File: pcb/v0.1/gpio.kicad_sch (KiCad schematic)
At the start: 36 parts, among them J7 ComputeModule5-CM5_connector, J8 Micro_SD_molex, J9 AudioJack3, SW1 SW_Push_45deg, U4 PCM5102A, U5 RT9742GGJ5, U6 RT9742GGJ5

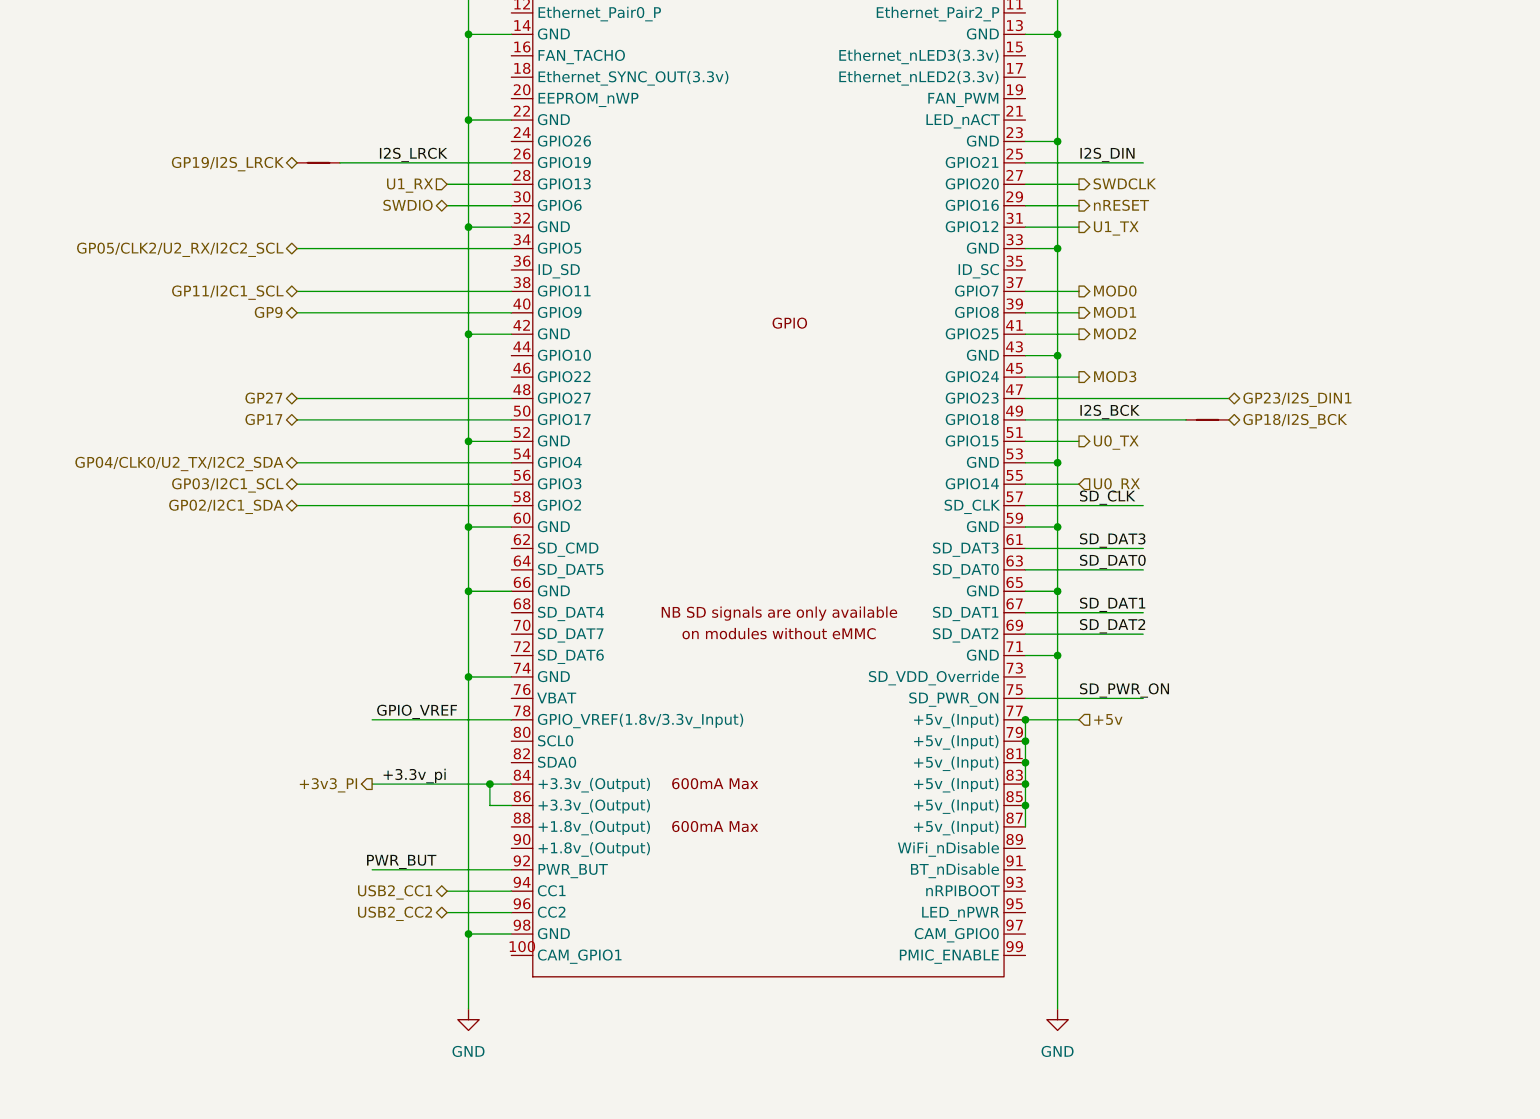
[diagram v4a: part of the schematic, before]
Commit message: Fix display connector wiring
Was not linked up with the i2c and CAM_GPIO pins from the gpio page.
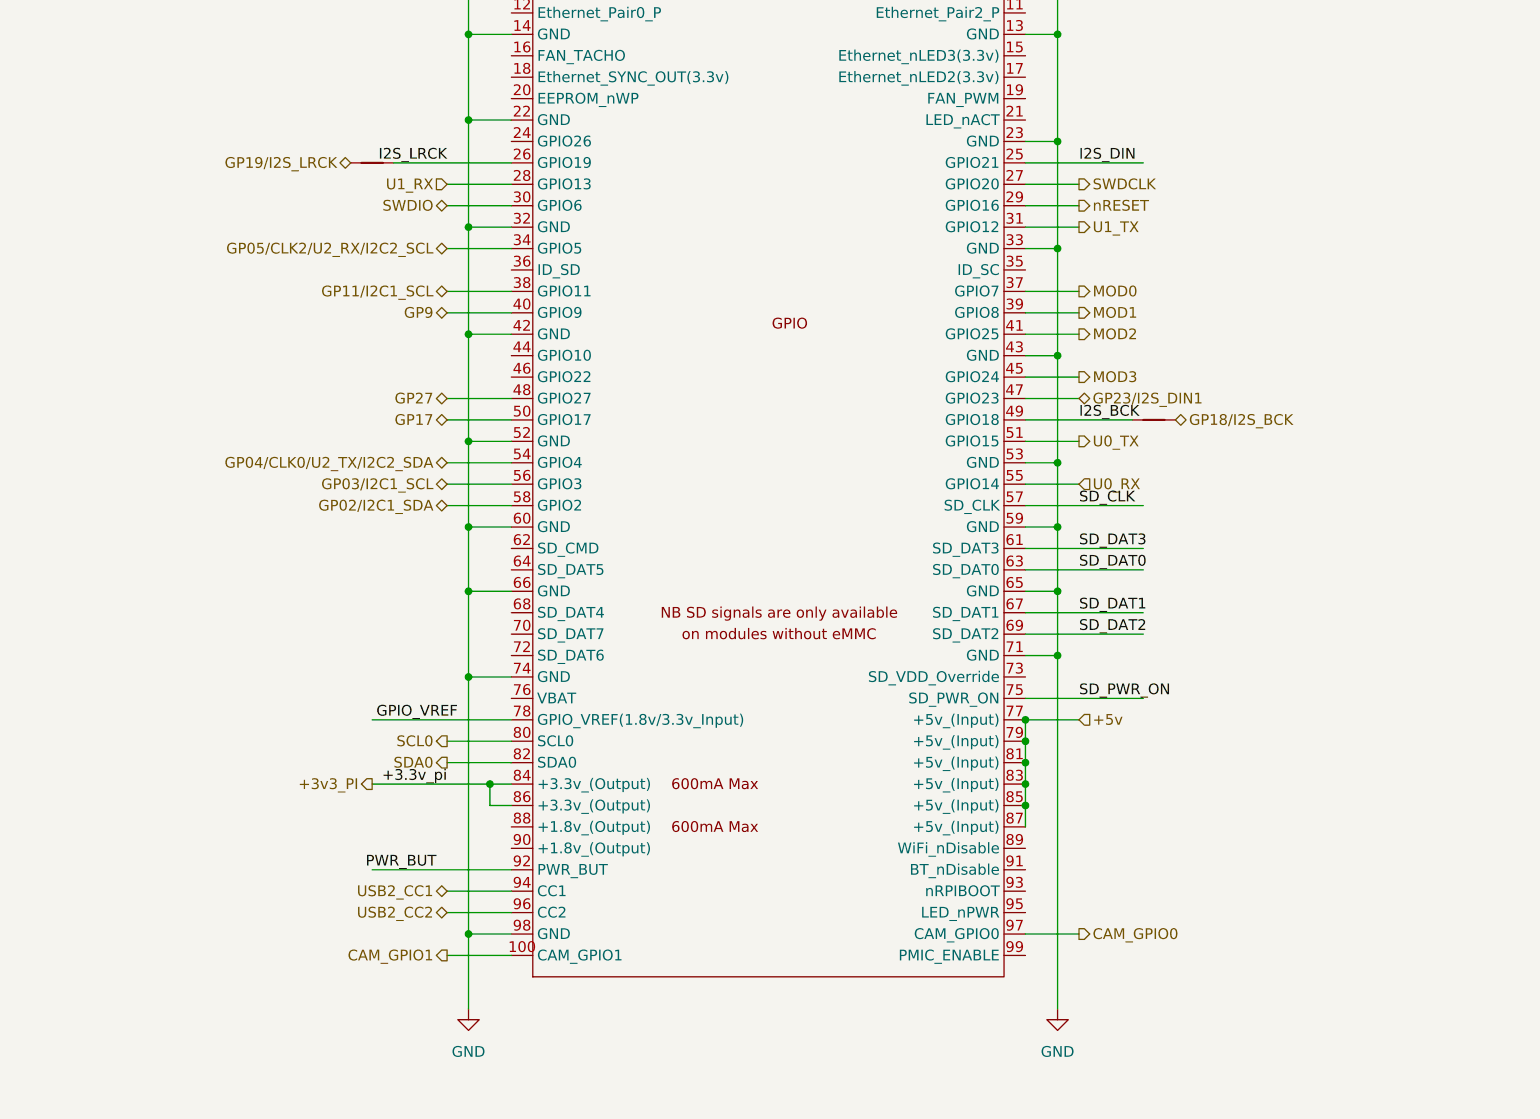
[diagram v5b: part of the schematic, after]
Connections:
- net CAM_GPIO1: now reaches J7.100 (CAM_GPIO1)
- net SCL0: now reaches J7.80 (SCL0)
- net SDA0: now reaches J7.82 (SDA0)
- net CAM_GPIO0: now reaches J7.97 (CAM_GPIO0)
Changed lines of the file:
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@@
 	(wire
 		(pts
-			(xy 69.85 124.46) (xy 95.25 124.46)
+			(xy 87.63 124.46) (xy 95.25 124.46)
 		)
 		(stroke
@@
 	(wire
 		(pts
-			(xy 74.93 93.98) (xy 95.25 93.98)
+			(xy 81.28 93.98) (xy 95.25 93.98)
 		)
 		(stroke
@@
 	(wire
 		(pts
+			(xy 87.63 187.96) (xy 95.25 187.96)
+		)
+		(stroke
+			(width 0)
+			(type default)
+		)
+	)
+	(wire
+		(pts
 			(xy 293.37 220.98) (xy 293.37 222.25)
 		)
@@
 	(wire
 		(pts
-			(xy 69.85 109.22) (xy 95.25 109.22)
+			(xy 87.63 109.22) (xy 95.25 109.22)
 		)
 		(stroke
@@
 	(wire
 		(pts
-			(xy 156.21 124.46) (xy 175.26 124.46)
+			(xy 156.21 124.46) (xy 168.91 124.46)
 		)
 		(stroke
@@
 	(wire
 		(pts
-			(xy 69.85 134.62) (xy 95.25 134.62)
+			(xy 87.63 134.62) (xy 95.25 134.62)
 		)
 		(stroke
@@
 	(wire
 		(pts
+			(xy 87.63 162.56) (xy 95.25 162.56)
+		)
+		(stroke
+			(width 0)
+			(type default)
+		)
+	)
+	(wire
+		(pts
 			(xy 300.99 203.2) (xy 309.88 203.2)
 		)
@@
 	(wire
 		(pts
+			(xy 156.21 185.42) (xy 162.56 185.42)
+		)
+		(stroke
+			(width 0)
+			(type default)
+		)
+	)
+	(wire
+		(pts
 			(xy 346.71 152.4) (xy 346.71 162.56)
 		)
@@
 	(wire
 		(pts
-			(xy 69.85 129.54) (xy 95.25 129.54)
+			(xy 87.63 129.54) (xy 95.25 129.54)
 		)
 		(stroke
@@
 	(wire
 		(pts
-			(xy 69.85 111.76) (xy 95.25 111.76)
+			(xy 87.63 111.76) (xy 95.25 111.76)
 		)
 		(stroke
@@
 	(wire
 		(pts
-			(xy 69.85 104.14) (xy 95.25 104.14)
+			(xy 87.63 104.14) (xy 95.25 104.14)
 		)
 		(stroke
@@
 	(wire
 		(pts
-			(xy 69.85 132.08) (xy 95.25 132.08)
+			(xy 87.63 132.08) (xy 95.25 132.08)
 		)
 		(stroke
@@
 	(wire
 		(pts
-			(xy 69.85 121.92) (xy 95.25 121.92)
+			(xy 87.63 121.92) (xy 95.25 121.92)
 		)
 		(stroke
@@
 	(wire
 		(pts
-			(xy 156.21 121.92) (xy 180.34 121.92)
+			(xy 156.21 121.92) (xy 162.56 121.92)
 		)
 		(stroke
@@
 	(wire
 		(pts
+			(xy 87.63 165.1) (xy 95.25 165.1)
+		)
+		(stroke
+			(width 0)
+			(type default)
+		)
+	)
+	(wire
+		(pts
 			(xy 369.57 104.14) (xy 369.57 106.68)
 		)
@@
 		)
 	)
+	(hierarchical_label "SDA0"
+		(shape output)
+		(at 87.63 165.1 180)
+		(effects
+			(font
+				(size 1.27 1.27)
+			)
+			(justify right)
+		)
+	)
 	(hierarchical_label "U1_TX"
 		(shape output)
@@
 		)
 	)
+	(hierarchical_label "CAM_GPIO1"
+		(shape output)
+		(at 87.63 187.96 180)
+		(effects
+			(font
+				(size 1.27 1.27)
+			)
+			(justify right)
+		)
+	)
 	(hierarchical_label "GP27"
 		(shape bidirectional)
-		(at 69.85 121.92 180)
+		(at 87.63 121.92 180)
 		(effects
 			(font
@@
 	(hierarchical_label "GP05{slash}CLK2{slash}U2_RX{slash}I2C2_SCL"
 		(shape bidirectional)
-		(at 69.85 104.14 180)
+		(at 87.63 104.14 180)
 		(effects
 			(font
@@
 	(hierarchical_label "GP9"
 		(shape bidirectional)
-		(at 69.85 111.76 180)
+		(at 87.63 111.76 180)
 		(effects
 			(font
@@
 	(hierarchical_label "GP11{slash}I2C1_SCL"
 		(shape bidirectional)
-		(at 69.85 109.22 180)
+		(at 87.63 109.22 180)
 		(effects
 			(font
@@
 	(hierarchical_label "GP02{slash}I2C1_SDA"
 		(shape bidirectional)
-		(at 69.85 134.62 180)
+		(at 87.63 134.62 180)
 		(effects
 			(font
@@
 	(hierarchical_label "GP18{slash}I2S_BCK"
 		(shape bidirectional)
-		(at 180.34 124.46 0)
+		(at 173.99 124.46 0)
 		(effects
 			(font
@@
 	(hierarchical_label "GP04{slash}CLK0{slash}U2_TX{slash}I2C2_SDA"
 		(shape bidirectional)
-		(at 69.85 129.54 180)
+		(at 87.63 129.54 180)
 		(effects
 			(font
@@
 	(hierarchical_label "GP17"
 		(shape bidirectional)
-		(at 69.85 124.46 180)
+		(at 87.63 124.46 180)
 		(effects
 			(font
@@
 		)
 	)
+	(hierarchical_label "SCL0"
+		(shape output)
+		(at 87.63 162.56 180)
+		(effects
+			(font
+				(size 1.27 1.27)
+			)
+			(justify right)
+		)
+	)
+	(hierarchical_label "CAM_GPIO0"
+		(shape output)
+		(at 162.56 185.42 0)
+		(effects
+			(font
+				(size 1.27 1.27)
+			)
+			(justify left)
+		)
+	)
 	(hierarchical_label "GP23{slash}I2S_DIN1"
 		(shape bidirectional)
-		(at 180.34 121.92 0)
+		(at 162.56 121.92 0)
 		(effects
 			(font
@@
 	(hierarchical_label "GP03{slash}I2C1_SCL"
 		(shape bidirectional)
-		(at 69.85 132.08 180)
+		(at 87.63 132.08 180)
 		(effects
 			(font
@@
 	(hierarchical_label "GP19{slash}I2S_LRCK"
 		(shape bidirectional)
-		(at 69.85 93.98 180)
+		(at 76.2 93.98 180)
 		(effects
 			(font
@@
 	(symbol
 		(lib_id "Device:NetTie_2")
-		(at 177.8 124.46 0)
+		(at 171.45 124.46 0)
 		(unit 1)
 		(body_style 1)
@@
 		(fields_autoplaced yes)
 		(property "Reference" "NT1"
-			(at 177.8 119.38 0)
+			(at 171.45 119.38 0)
 			(hide yes)
 			(show_name no)
@@
 		)
 		(property "Value" "NetTie_2"
-			(at 177.8 121.92 0)
+			(at 171.45 121.92 0)
 			(hide yes)
 			(show_name no)
@@
 		)
 		(property "Footprint" ""
-			(at 177.8 124.46 0)
+			(at 171.45 124.46 0)
 			(hide yes)
 			(show_name no)
@@
 		)
 		(property "Datasheet" ""
-			(at 177.8 124.46 0)
+			(at 171.45 124.46 0)
 			(hide yes)
 			(show_name no)
@@
 		)
 		(property "Description" "Net tie, 2 pins"
-			(at 177.8 124.46 0)
+			(at 171.45 124.46 0)
 			(hide yes)
 			(show_name no)
@@
 	(symbol
 		(lib_id "Device:NetTie_2")
-		(at 72.39 93.98 0)
+		(at 78.74 93.98 0)
 		(mirror y)
 		(unit 1)
@@
 		(fields_autoplaced yes)
 		(property "Reference" "NT2"
-			(at 72.39 88.9 0)
+			(at 78.74 88.9 0)
 			(hide yes)
 			(show_name no)
@@
 		)
 		(property "Value" "NetTie_2"
-			(at 72.39 91.44 0)
+			(at 78.74 91.44 0)
 			(hide yes)
 			(show_name no)
@@
 		)
 		(property "Footprint" ""
-			(at 72.39 93.98 0)
+			(at 78.74 93.98 0)
 			(hide yes)
 			(show_name no)
@@
 		)
 		(property "Datasheet" ""
-			(at 72.39 93.98 0)
+			(at 78.74 93.98 0)
 			(hide yes)
 			(show_name no)
@@
 		)
 		(property "Description" "Net tie, 2 pins"
-			(at 72.39 93.98 0)
+			(at 78.74 93.98 0)
 			(hide yes)
 			(show_name no)

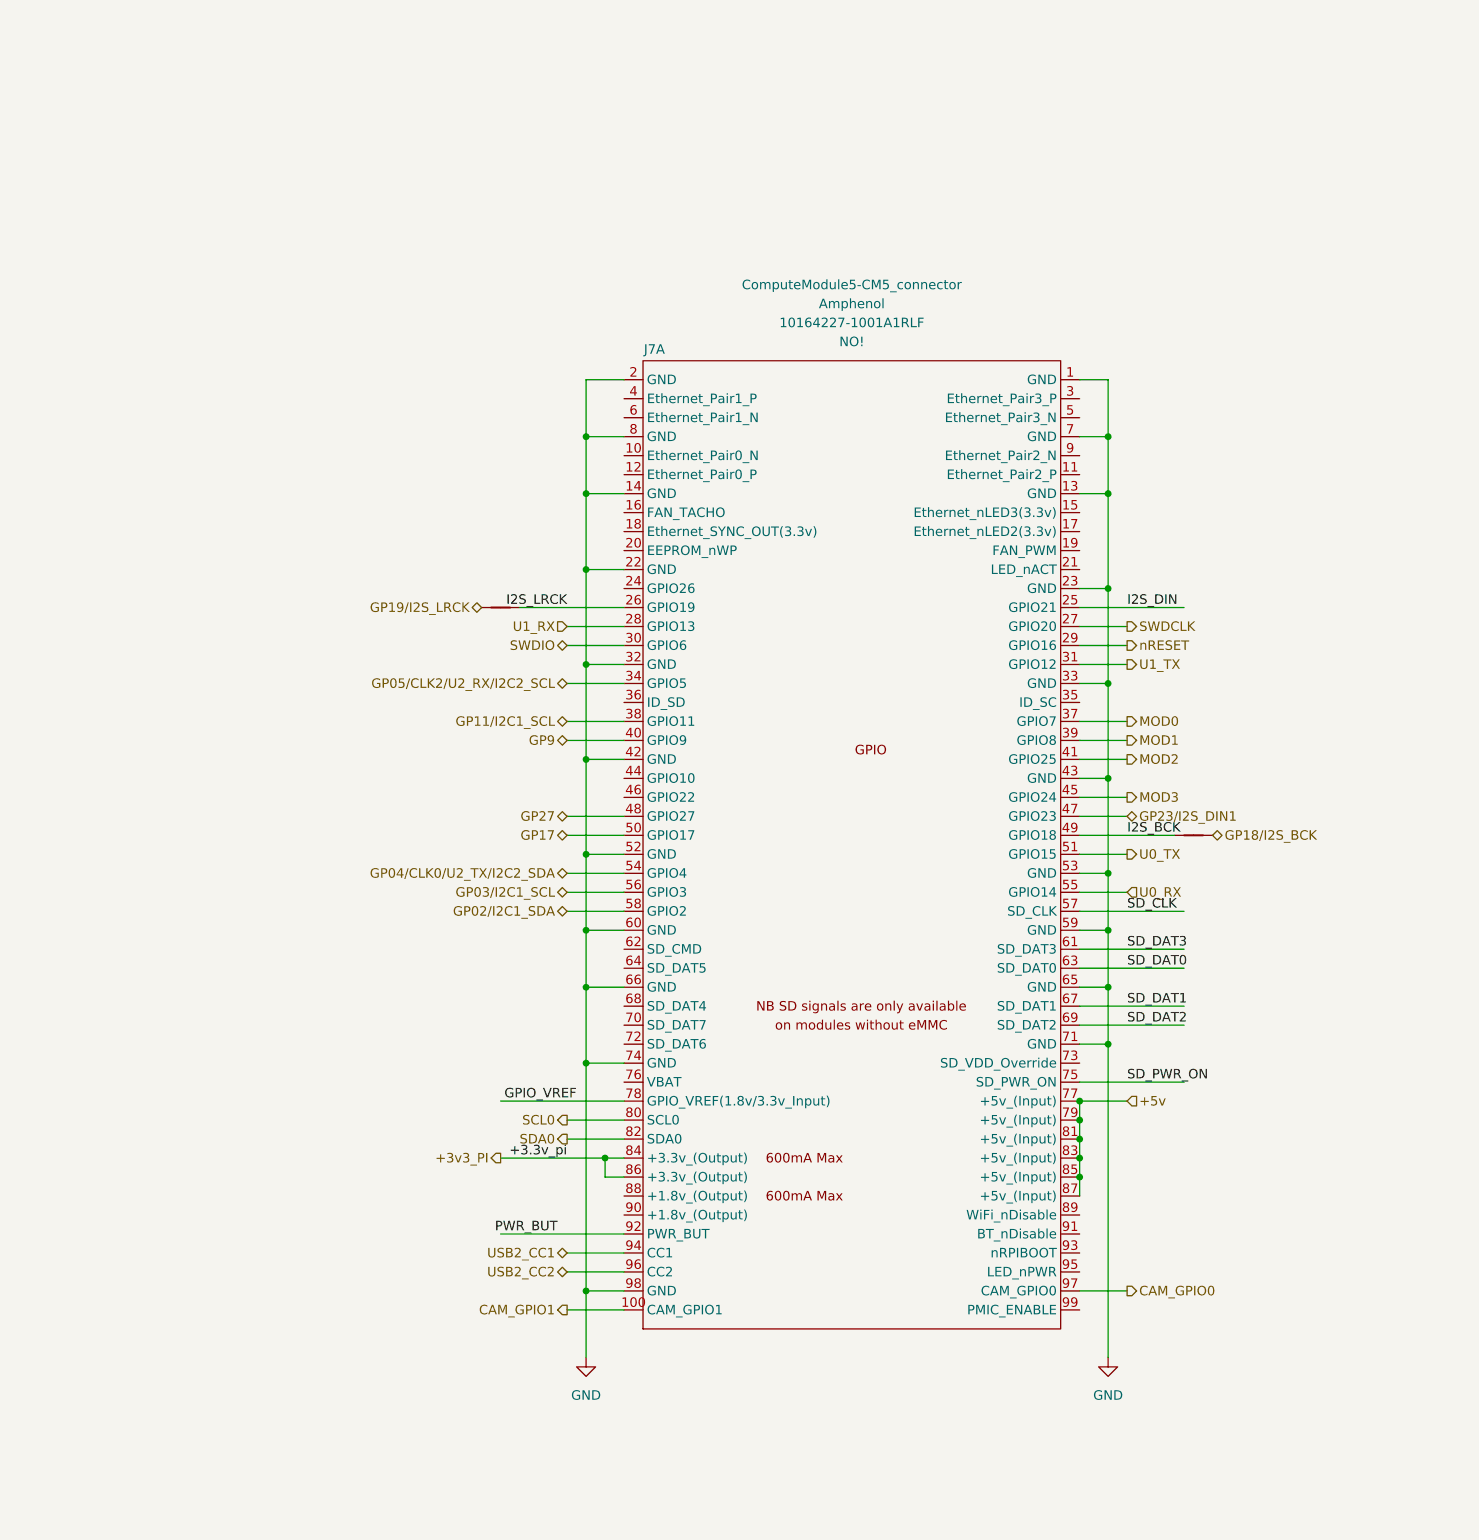
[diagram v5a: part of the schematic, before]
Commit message: High speed and Super speed ESD arrays
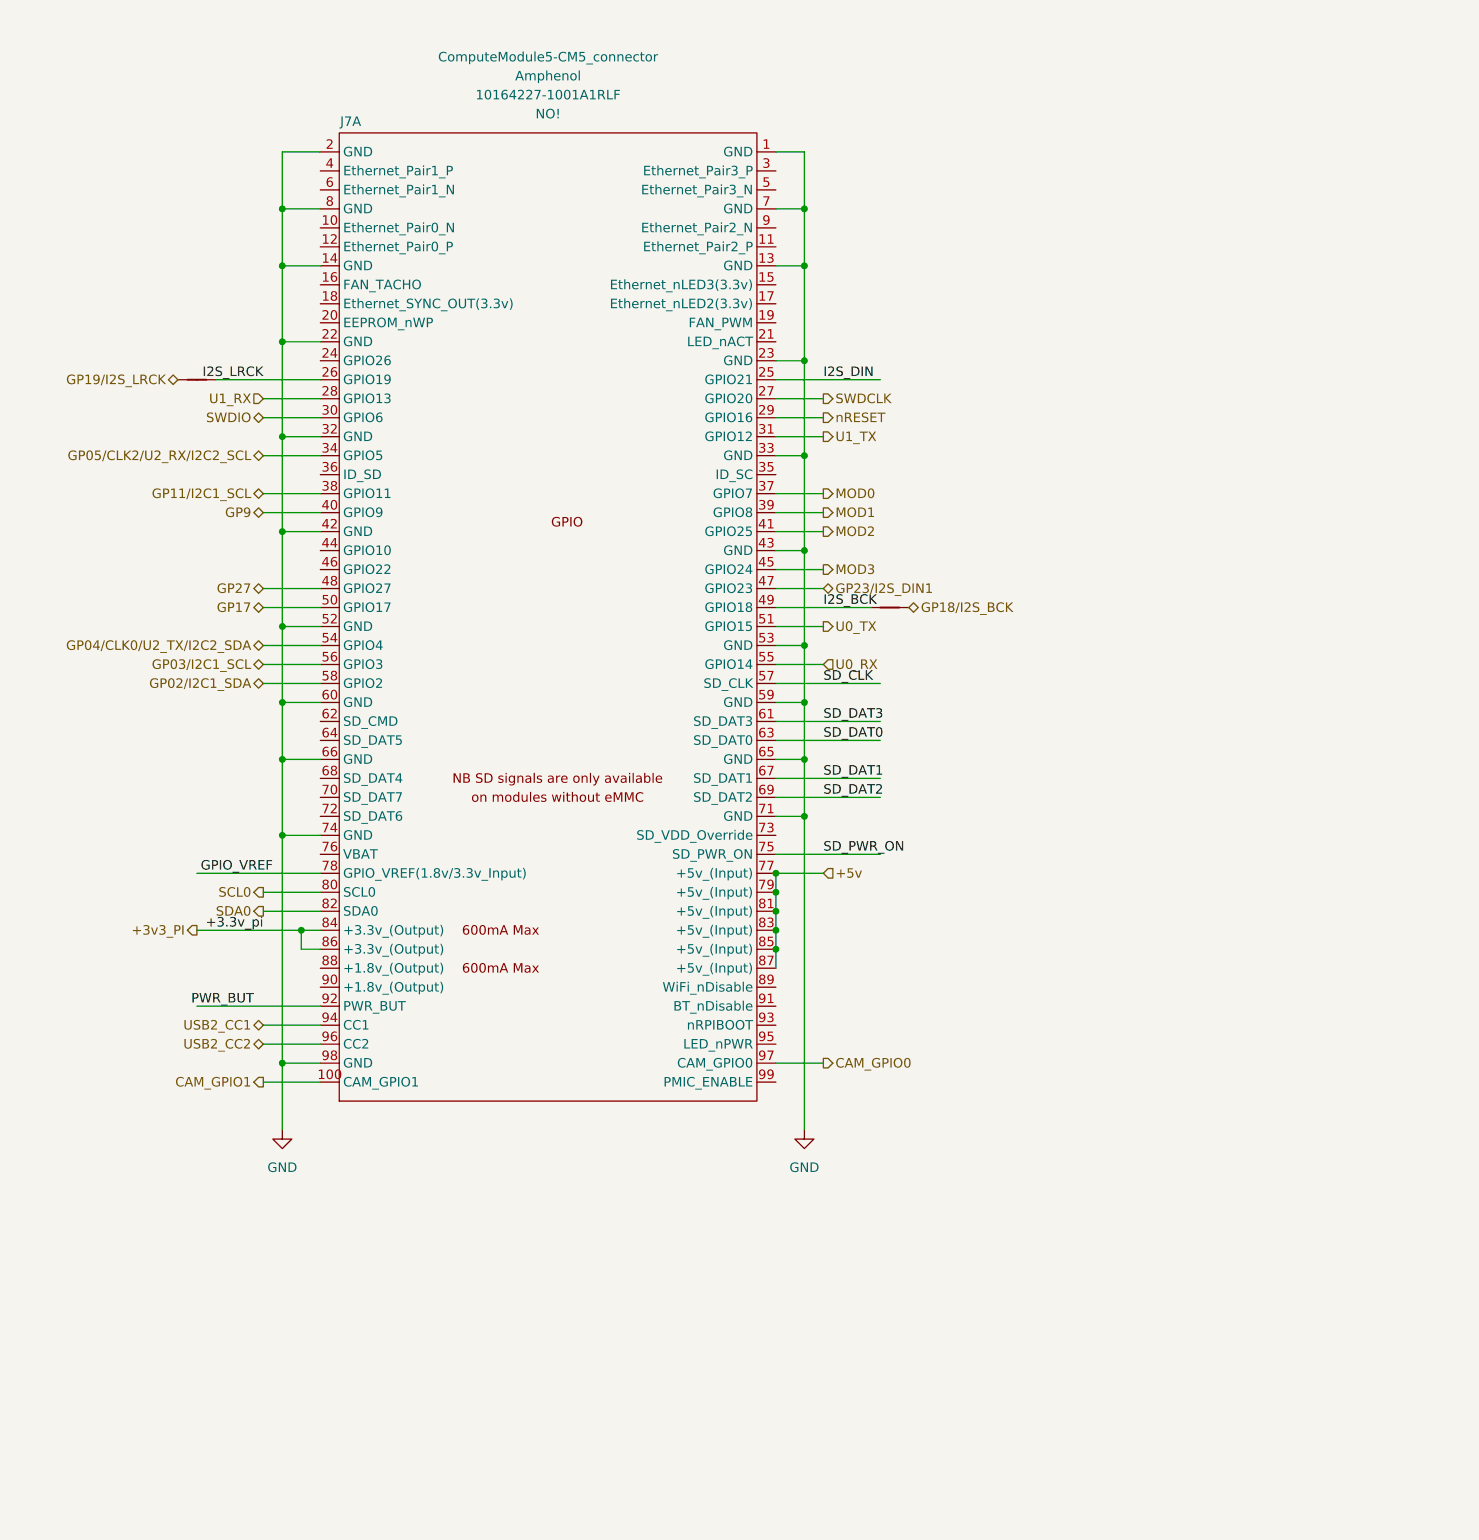
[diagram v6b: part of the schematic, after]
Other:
- moved on the sheet: J7A
